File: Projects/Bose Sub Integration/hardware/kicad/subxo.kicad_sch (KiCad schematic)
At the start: 43 parts, among them J1 IN L, J2 IN R, J3 OUT 3.5mm, J4 PWR IN 15V, J5 POLARITY SW, J6 LEVEL POT 10k, J7 INV LED, U1 TL074, U2 LM7812

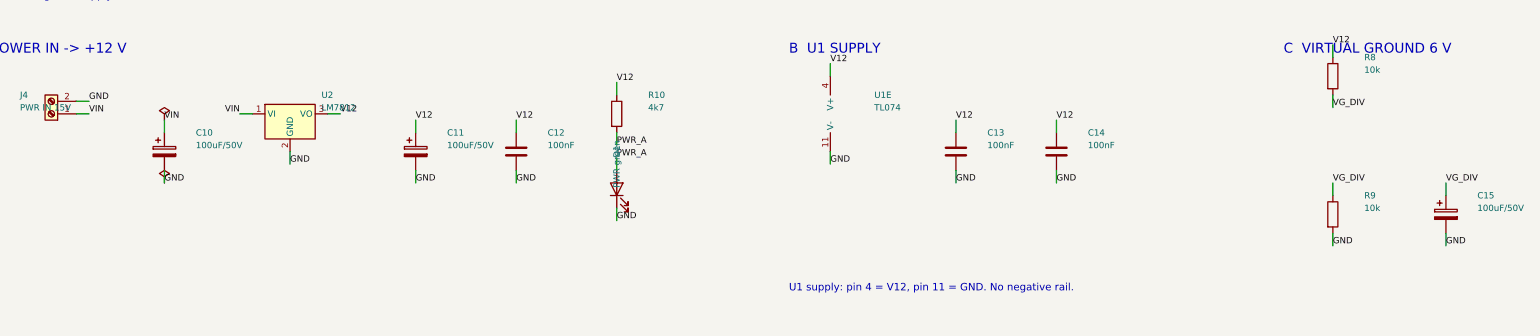
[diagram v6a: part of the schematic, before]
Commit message: Sub crossover: bridge the split ground pour with a wire link
The GND pour fills as two islands. The power corner -- J4, U2, C10 to C14, R9 --
is walled off from the rest of the board by the ring of parts around it. The two
come within 2.70 mm of each other beside U2.3, close enough to be worth trying
to close, so I moved U2 by plus and minus 3 mm in both axes and re-filled: still
two islands every time. The wall is the whole component ring, not that one pad.

So LK1 bridges them on an insulated wire, and GND splits into GND and GND_LNK to
match. The split is what makes a wire link work at all -- with one net on both
pads KiCad cannot know the wire is there and keeps reporting the island. Net
membership is taken from KiCad's own zone fill rather than guessed, and it is
placement-dependent: move parts and it has to be re-derived.

Each segment now carries its own PWR_FLAG, or ERC calls it undriven. And two
ground nets means two zones, since island_removal_mode 0 would otherwise delete
the power corner as an island with no pad of the zone's net.

Also withdrew the dual-pitch C_in footprint added earlier today. Its two
same-numbered pads sat 5 mm apart with no copper joining them; stock multi-pitch
footprints only work because their alternate pads overlap into one blob, and
duplicate_pad_numbers_are_jumpers defaults to no with no stock footprint in
KiCad 10 setting it. It bought nothing either, because a 2u2 film is 15 mm pitch
like the 220n, so the plain stock footprint rev A already had covers both.

ERC 0 errors, verify_netlist 118 of 118.
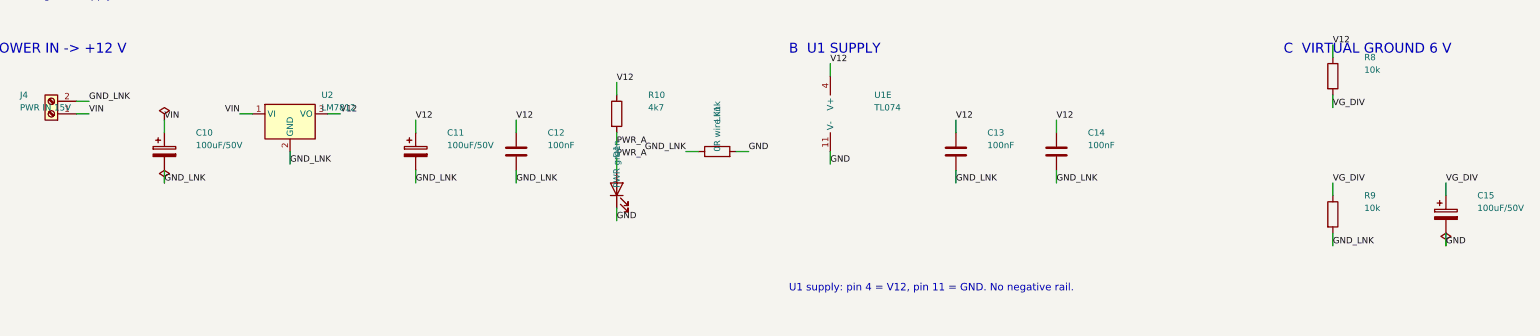
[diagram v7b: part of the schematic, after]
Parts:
- added LK1: 0R wire link, energy_system:WireLink_P14.50mm, symbol Device:R
- C_in1, C_in2: footprint energy_system:C_Rect_L18.0mm_W9.0mm_P5.00mm_P15.00mm_MultiPitch -> Capacitor_THT:C_Rect_L18.0mm_W9.0mm_P15.00mm_FKS3_FKP3
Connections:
- net GND: now also LK1.2; no longer C10.2, C11.2, C12.2, C13.2, C14.2, J4.2 (Pin_2), R9.2, U2.2 (GND)
- new net GND_LNK: C10.2, C11.2, C12.2, C13.2, C14.2, J4.2 (Pin_2), LK1.1, R9.2, U2.2 (GND)
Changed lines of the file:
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@@
 	(symbol
 		(lib_id "Device:R")
+		(at 190.5 63.5 90)
+		(unit 1)
+		(exclude_from_sim no)
+		(in_bom yes)
+		(on_board yes)
+		(dnp no)
+		(property "Reference" "LK1"
+			(at 190.5 55.88 0)
+			(effects
+				(font
+					(size 1.27 1.27)
+				)
+			)
+		)
+		(property "Value" "0R wire link"
+			(at 190.5 58.42 0)
+			(effects
+				(font
+					(size 1.27 1.27)
+				)
+			)
+		)
+		(property "Footprint" "energy_system:WireLink_P14.50mm"
+			(at 190.5 63.5 0)
+			(effects
+				(font
+					(size 1.27 1.27)
+				)
+				(hide yes)
+			)
+		)
+		(property "Datasheet" "~"
+			(at 190.5 63.5 0)
+			(effects
+				(font
+					(size 1.27 1.27)
+				)
+				(hide yes)
+			)
+		)
+		(property "Description" ""
+			(at 190.5 63.5 0)
+			(effects
+				(font
+					(size 1.27 1.27)
+				)
+				(hide yes)
+			)
+		)
+		(pin "1"
+		)
+		(pin "2"
+		)
+		(instances
+			(project "subxo"
+				(path "/b05e5ub0-0001-0001-0001-000000000001"
+					(reference "LK1")
+					(unit 1)
+				)
+			)
+		)
+	)
+	(symbol
+		(lib_id "Device:R")
 		(at 170.18 55.88 0)
 		(unit 1)
@@
 			)
 		)
-		(property "Footprint" "energy_system:C_Rect_L18.0mm_W9.0mm_P5.00mm_P15.00mm_MultiPitch"
+		(property "Footprint" "Capacitor_THT:C_Rect_L18.0mm_W9.0mm_P15.00mm_FKS3_FKP3"
 			(at 83.82 160.02 0)
 			(effects
@@
 			)
 		)
-		(property "Footprint" "energy_system:C_Rect_L18.0mm_W9.0mm_P5.00mm_P15.00mm_MultiPitch"
+		(property "Footprint" "Capacitor_THT:C_Rect_L18.0mm_W9.0mm_P15.00mm_FKS3_FKP3"
 			(at 83.82 236.22 0)
 			(effects
@@
 		)
 	)
-	(label "GND"
+	(label "GND_LNK"
 		(at 63.5 53.34 0)
 		(effects
@@
 		)
 	)
-	(label "GND"
+	(label "GND_LNK"
 		(at 78.74 69.85 0)
 		(effects
@@
 		)
 	)
-	(label "GND"
+	(label "GND_LNK"
 		(at 104.14 66.04 0)
 		(effects
@@
 		)
 	)
-	(label "GND"
+	(label "GND_LNK"
 		(at 129.54 69.85 0)
 		(effects
@@
 		)
 	)
-	(label "GND"
+	(label "GND_LNK"
 		(at 149.86 69.85 0)
 		(effects
@@
 		)
 	)
-	(label "GND"
+	(label "GND_LNK"
 		(at 238.76 69.85 0)
 		(effects
@@
 		)
 	)
-	(label "GND"
+	(label "GND_LNK"
 		(at 259.08 69.85 0)
 		(effects
@@
 		)
 	)
-	(label "GND"
+	(label "GND_LNK"
 		(at 314.96 82.55 0)
 		(effects
@@
 	(wire
 		(pts
+			(xy 186.69 63.5) (xy 184.15 63.5)
+		)
+		(stroke
+			(width 0)
+			(type default)
+		)
+	)
+	(label "GND_LNK"
+		(at 184.15 63.5 0)
+		(effects
+			(font
+				(size 1.27 1.27)
+			)
+			(justify right bottom)
+		)
+	)
+	(wire
+		(pts
+			(xy 194.31 63.5) (xy 196.85 63.5)
+		)
+		(stroke
+			(width 0)
+			(type default)
+		)
+	)
+	(label "GND"
+		(at 196.85 63.5 0)
+		(effects
+			(font
+				(size 1.27 1.27)
+			)
+			(justify left bottom)
+		)
+	)
+	(wire
+		(pts
 			(xy 60.96 160.02) (xy 63.5 160.02)
 		)
@@
 					(unit 1)
 				)
+			)
+		)
+	)
+	(symbol
+		(lib_id "power:PWR_FLAG")
+		(at 337.82 82.55 0)
+		(unit 1)
+		(exclude_from_sim no)
+		(in_bom yes)
+		(on_board yes)
+		(dnp no)
+		(property "Reference" "#FLG003"
+			(at 337.82 80.01 0)
+			(effects
+				(font
+					(size 1.27 1.27)
+				)
+				(hide yes)
+			)
+		)
+		(property "Value" "PWR_FLAG"
+			(at 337.82 77.47 0)
+			(effects
+				(font
+					(size 1.27 1.27)
+				)
+				(hide yes)
+			)
+		)
+		(property "Footprint" ""
+			(at 337.82 82.55 0)
+			(effects
+				(font
+					(size 1.27 1.27)
+				)
+				(hide yes)
+			)
+		)
+		(property "Datasheet" ""
+			(at 337.82 82.55 0)
+			(effects
+				(font
+					(size 1.27 1.27)
+				)
+				(hide yes)
+			)
+		)
+		(pin "1"
+		)
+		(instances
+			(project "subxo"
+				(path "/b05e5ub0-0001-0001-0001-000000000001"
+					(reference "#FLG003")
+					(unit 1)
+				)

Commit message: Sub crossover: widen the LED footprint so it clears the milling rule
The only real DRC errors on the hand-placed board were the two status LEDs:
2.54 mm pitch against 1.8 mm pads leaves 0.74 mm between them, under the
0.85 mm rule and nowhere near the 1.2 mm a 0.8 mm endmill would want. Four
violations, two per LED, reported once from each side.

There is no stock footprint to switch to. Every two-pad part in LED_THT uses the
same 2.54/1.8 geometry, so this is a project footprint.

LED legs bend freely, so the pitch is the lever to pull rather than the pad
size -- the opposite of the TO-220, whose pitch is fixed and whose pads had to
be narrowed to 1.7 mm instead. 5.08 mm pitch with 2.0 mm pads gives a 3.08 mm
channel, which clears either process with room to spare and leaves a generous
annular ring for milling. 2.54 mm of total splay is nothing for an LED.

Drill stays 0.8 mm, already the commonest size on the board.
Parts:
- D1, D2: footprint LED_THT:LED_D3.0mm -> energy_system:LED_D3.0mm_P5.08mm_LaserPads
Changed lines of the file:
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@@
 			)
 		)
-		(property "Footprint" "LED_THT:LED_D3.0mm"
+		(property "Footprint" "energy_system:LED_D3.0mm_P5.08mm_LaserPads"
 			(at 170.18 71.12 0)
 			(effects
@@
 			)
 		)
-		(property "Footprint" "LED_THT:LED_D3.0mm"
+		(property "Footprint" "energy_system:LED_D3.0mm_P5.08mm_LaserPads"
 			(at 520.7 317.5 0)
 			(effects
